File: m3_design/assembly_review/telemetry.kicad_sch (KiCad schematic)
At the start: 26 parts, among them J410 GPS 4V8/GND/TX/RX, J420 RADIO 4V8/GND/TX/RX, U411 TXU0202DCUR, U412 TPS70933DBVR, U421 TXU0202DCUR, U422 TPS70933DBVR

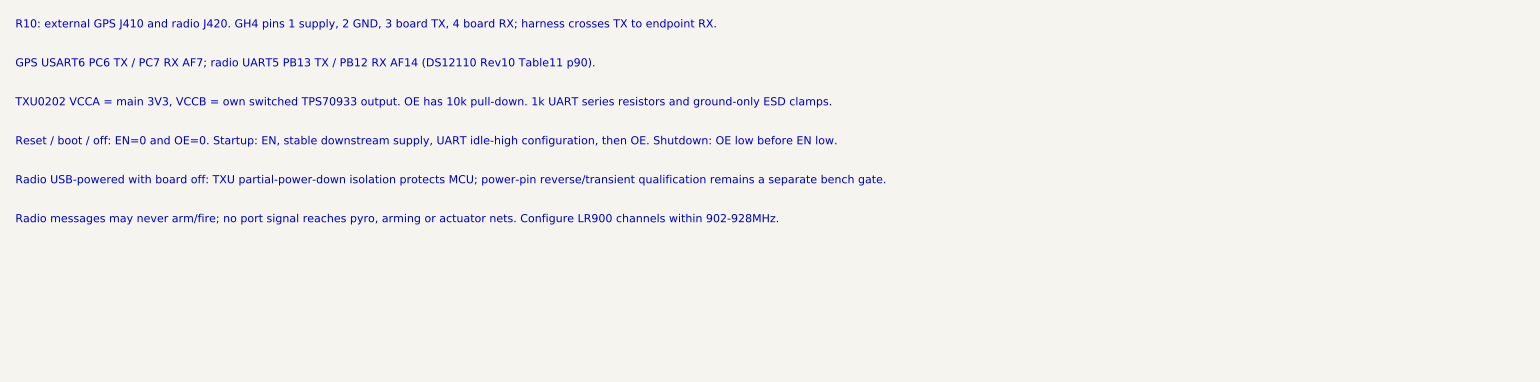
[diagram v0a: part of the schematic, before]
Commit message: R10 review round 3 and fix pass: ten-lens review of 883d2db5 (0 Critical, 7 Major, 49 Minor); In2 GND under the pyro column (S-8), U9 power path widened, In2 re-cut for the port control nets, GND vias at port-signal layer changes, crystal In2 GND restored, stitching, silkscreen >= 0.15 mm; gates: arcs, K-loader, S-8/S-9, wider critical set, needless hops, plate masses; R410 budget, R162 1k, F6 ride-through restated (OQ-5/OQ-6); board 579575bd..., check.sh 0
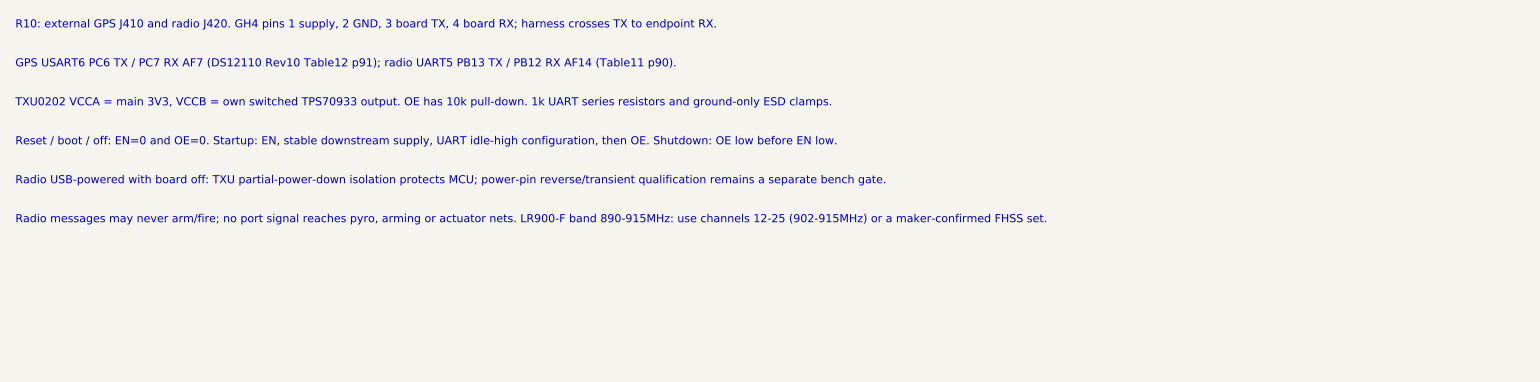
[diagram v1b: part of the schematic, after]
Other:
- note added: "GPS USART6 PC6 TX / PC7 RX AF7 (DS12110 Rev10 Table12 p91); radio UART5 PB13 TX / PB12 RX AF14 (Table11 p90)."
- note added: "Radio messages may never arm/fire; no port signal reaches pyro, arming or actuator nets. LR900-F band 890-915MHz: use channels 12-25 (902-915MHz) or a maker-confirmed FHSS set."
- note removed: "GPS USART6 PC6 TX / PC7 RX AF7; radio UART5 PB13 TX / PB12 RX AF14 (DS12110 Rev10 Table11 p90)."
- note removed: "Radio messages may never arm/fire; no port signal reaches pyro, arming or actuator nets. Configure LR900 channels within 902-928MHz."
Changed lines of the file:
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@@
 			(justify left))
 )
-	(text "GPS USART6 PC6 TX / PC7 RX AF7; radio UART5 PB13 TX / PB12 RX AF14 (DS12110 Rev10 Table11 p90)."
+	(text "GPS USART6 PC6 TX / PC7 RX AF7 (DS12110 Rev10 Table12 p91); radio UART5 PB13 TX / PB12 RX AF14 (Table11 p90)."
 		(at 20.32 20.32 0)
 		(effects
@@
 			(justify left))
 )
-	(text "Radio messages may never arm/fire; no port signal reaches pyro, arming or actuator nets. Configure LR900 channels within 902-928MHz."
+	(text "Radio messages may never arm/fire; no port signal reaches pyro, arming or actuator nets. LR900-F band 890-915MHz: use channels 12-25 (902-915MHz) or a maker-confirmed FHSS set."
 		(at 20.32 40.64 0)
 		(effects
